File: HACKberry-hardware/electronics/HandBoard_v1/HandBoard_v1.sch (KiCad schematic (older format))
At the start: 11 parts, among them CON1 BARREL_JACK_MJ179PH, SW1 SW_PUSH_SKRGAQD010, SW2 SW_PUSH_SKRGAQD010, SW3 SW_PUSH_SKRGAQD010, SW4 SWITCH_INV, U2 3-CONDUCTOR_MINIATUIRE_JACK_M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, U3 Arduino_Micro, U4 Seed_Studio_Adjustable_DC/DC_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, U5 Servo_Motor_MG90S, U6 Servo_Motor_S03N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

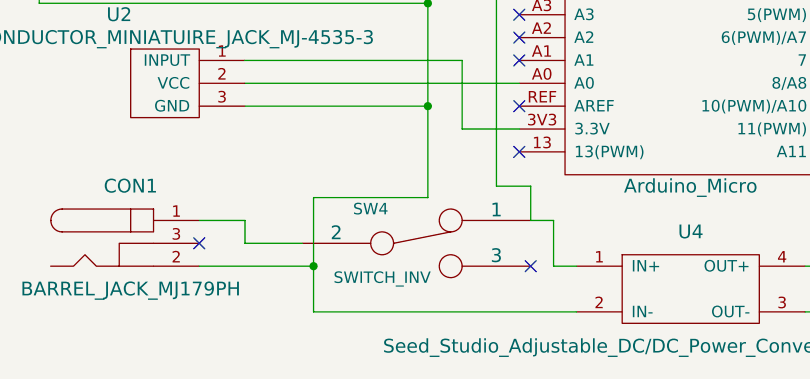
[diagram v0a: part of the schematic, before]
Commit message: rivice of the schematic
add the parts name of slide switch
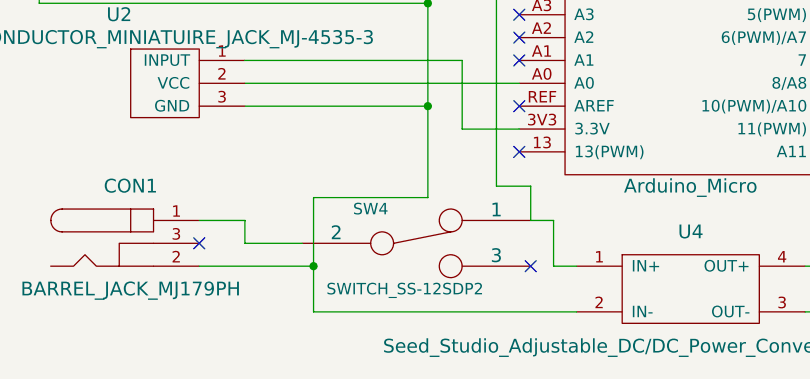
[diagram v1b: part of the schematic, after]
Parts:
- SW4: value SWITCH_INV -> SWITCH_SS-12SDP2
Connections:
- net at U3.GND: now also CON1.2, SW1.1, SW2.1, SW3.1, U2.3 (GND), U4.2 (IN-)
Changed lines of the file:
@@
 LIBS:yamaura
 LIBS:arduino
-LIBS:HandBoard_v1-cache
 EELAYER 25 0
 EELAYER END
@@
 P 4300 5200
 F 0 "SW4" H 4100 5350 50  0000 C CNN
-F 1 "SWITCH_INV" H 4150 5050 50  0000 C CNN
+F 1 "SWITCH_SS-12SDP2" H 4250 5000 50  0000 C CNN
 F 2 "" H 4300 5200 60  0000 C CNN
 F 3 "" H 4300 5200 60  0000 C CNN

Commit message: bug fix
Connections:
- net at U3.3V3 (3.3V): now also U2.2 (VCC); no longer U2.1 (INPUT)
- net at U3.A0: now also U2.1 (INPUT); no longer U2.2 (VCC)
- net at U3.GND: now also CON1.2, SW1.1, SW2.1, SW3.1, U2.3 (GND), U4.2 (IN-)
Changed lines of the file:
@@
 LIBS:yamaura
 LIBS:arduino
+LIBS:HandBoard_v1-cache
 EELAYER 25 0
 EELAYER END
@@
 	6800 4550 7650 4550
 Wire Wire Line
-	3550 4500 4750 4500
-Wire Wire Line
 	3850 5000 3850 5500
 Wire Wire Line
@@
 Connection ~ 3850 5300
 Connection ~ 4350 4600
-Wire Wire Line
-	3550 4400 4500 4400
-Wire Wire Line
-	4500 4400 4500 4700
-Wire Wire Line
-	4500 4700 4750 4700
 Wire Wire Line
 	2900 3200 2650 3200
@@
 	3550 5200 3800 5200
 NoConn ~ 3350 5200
+Wire Wire Line
+	3550 4500 4450 4500
+Wire Wire Line
+	4450 4500 4450 4700
+Wire Wire Line
+	4450 4700 4750 4700
+Wire Wire Line
+	3550 4400 4550 4400
+Wire Wire Line
+	4550 4400 4550 4500
+Wire Wire Line
+	4550 4500 4750 4500
 $EndSCHEMATC

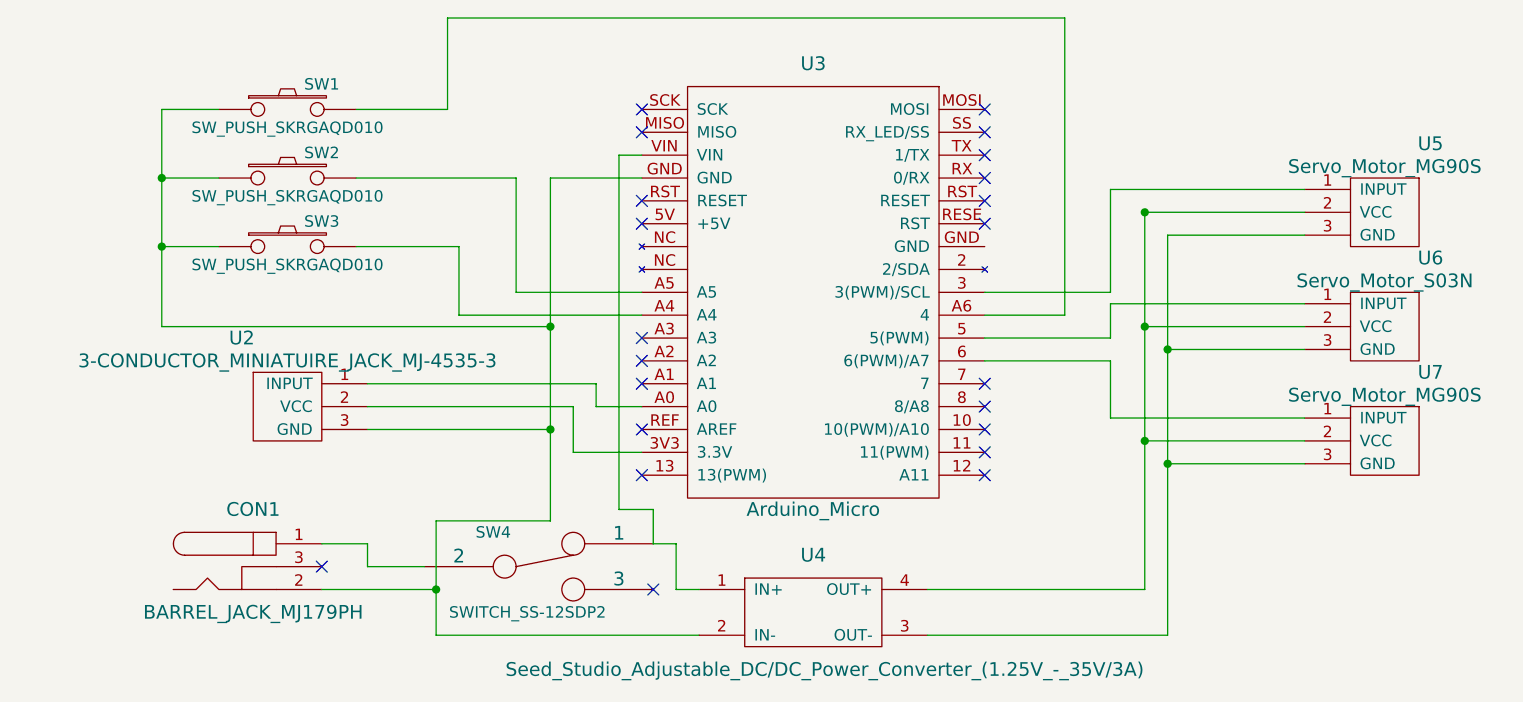
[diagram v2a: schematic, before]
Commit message: Fixed incorrect appearance in schematic
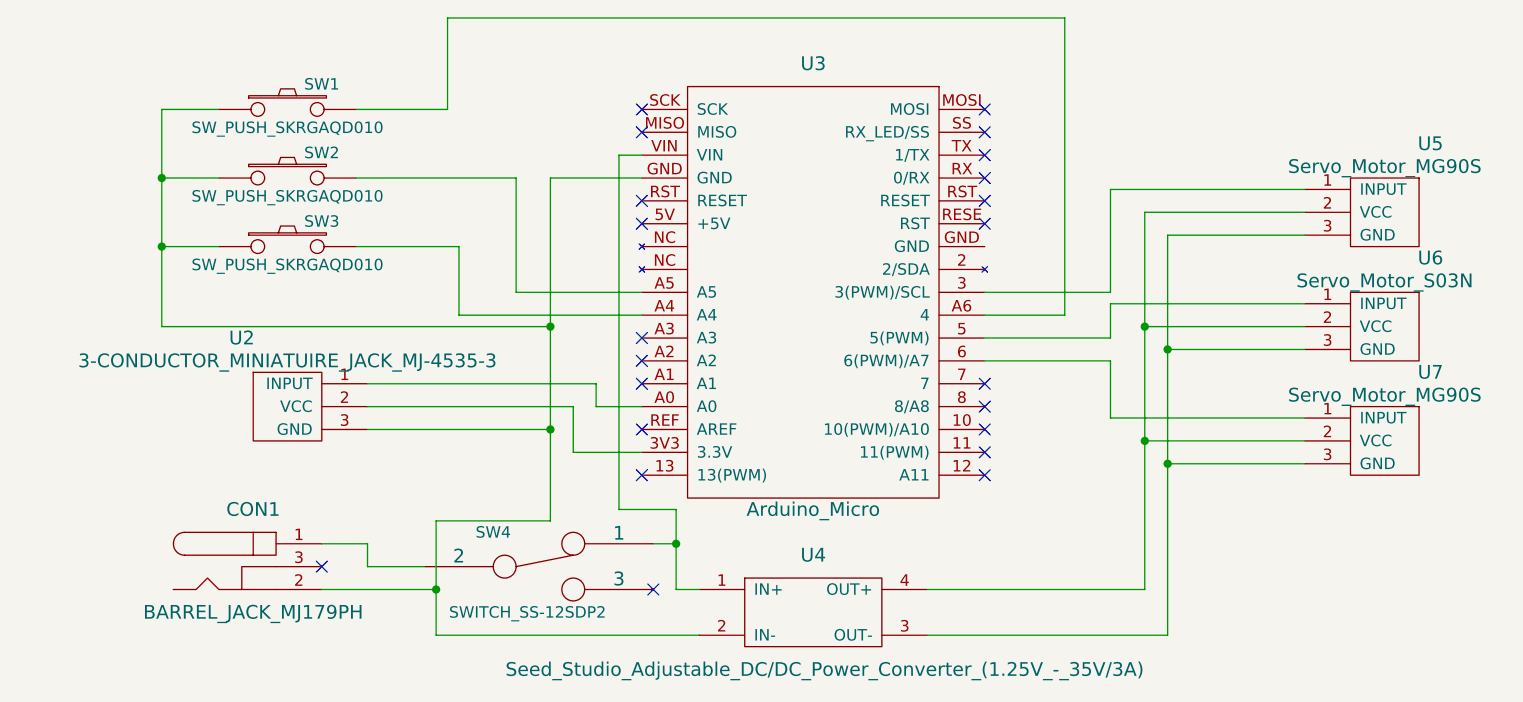
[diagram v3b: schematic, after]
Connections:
- net at U3.GND: now also CON1.2, SW1.1, SW2.1, SW3.1, U2.3 (GND), U4.2 (IN-)
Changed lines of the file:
@@
 LIBS:contrib
 LIBS:valves
-LIBS:yamaura
 LIBS:arduino
 LIBS:HandBoard_v1-cache
@@
 Wire Wire Line
 	6950 4150 7650 4150
-Connection ~ 6950 3650
 Wire Wire Line
 	6950 4650 7650 4650
@@
 	4800 5100 4900 5100
 Wire Wire Line
-	4900 5100 4900 5300
+	4900 4950 4900 5300
 Wire Wire Line
 	4900 5300 5000 5300
 Wire Wire Line
-	4800 5100 4800 4950
-Wire Wire Line
-	4800 4950 4650 4950
+	4650 4950 4900 4950
 Wire Wire Line
 	4650 4950 4650 3400
@@
 Wire Wire Line
 	4550 4500 4750 4500
+Connection ~ 4900 5100
 $EndSCHEMATC

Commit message: Revert "Fixed incorrect appearance in schematic"
This reverts commit 3b6817b660281c2eda156baa4225a43203330258.
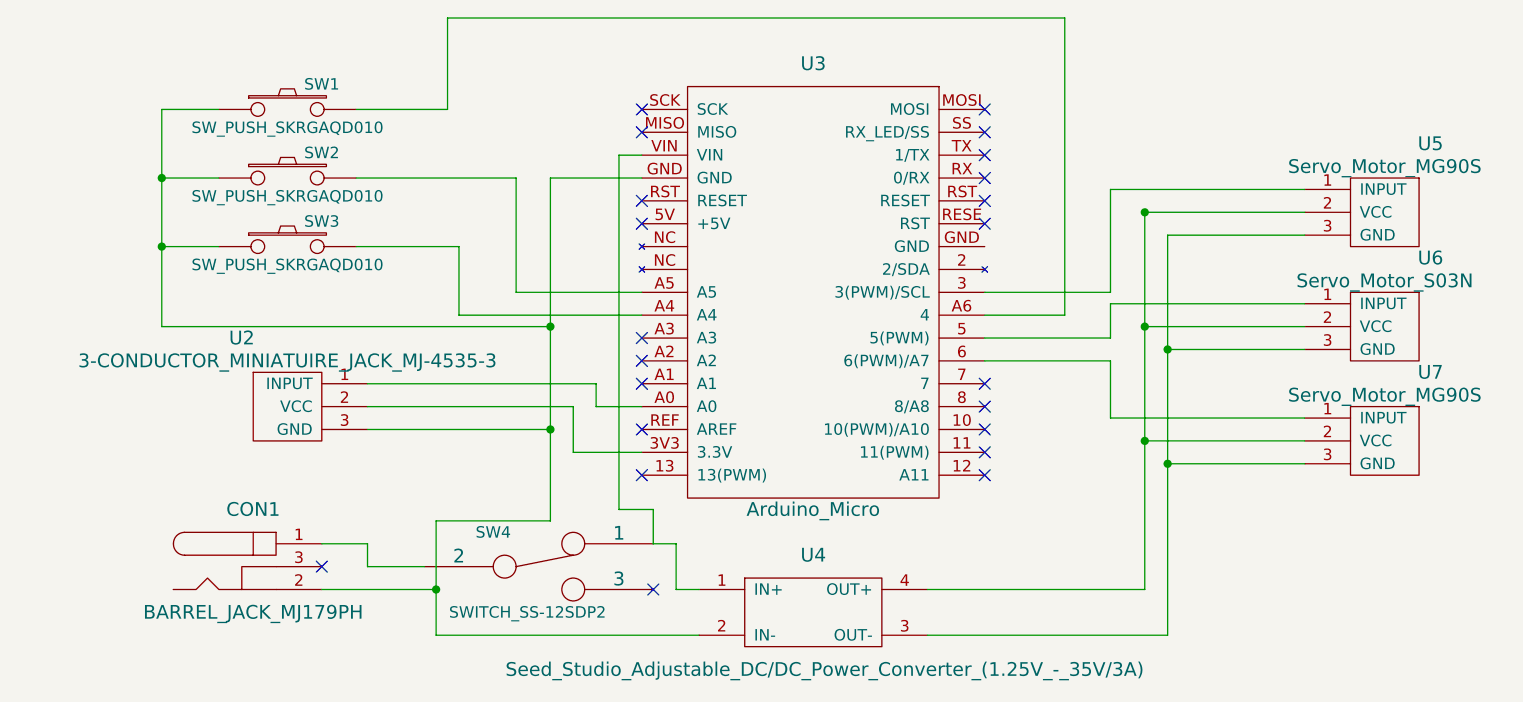
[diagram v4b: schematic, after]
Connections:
- net at U3.GND: now also CON1.2, SW1.1, SW2.1, SW3.1, U2.3 (GND), U4.2 (IN-)
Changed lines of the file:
@@
 LIBS:contrib
 LIBS:valves
+LIBS:yamaura
 LIBS:arduino
 LIBS:HandBoard_v1-cache
@@
 Wire Wire Line
 	6950 4150 7650 4150
+Connection ~ 6950 3650
 Wire Wire Line
 	6950 4650 7650 4650
@@
 	4800 5100 4900 5100
 Wire Wire Line
-	4900 4950 4900 5300
+	4900 5100 4900 5300
 Wire Wire Line
 	4900 5300 5000 5300
 Wire Wire Line
-	4650 4950 4900 4950
+	4800 5100 4800 4950
+Wire Wire Line
+	4800 4950 4650 4950
 Wire Wire Line
 	4650 4950 4650 3400
@@
 Wire Wire Line
 	4550 4500 4750 4500
-Connection ~ 4900 5100
 $EndSCHEMATC
